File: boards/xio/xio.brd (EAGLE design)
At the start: 170 x 100 mm, 151 parts, among them Y2 NX3225SA-12.000MHZ-STD-CSR-1

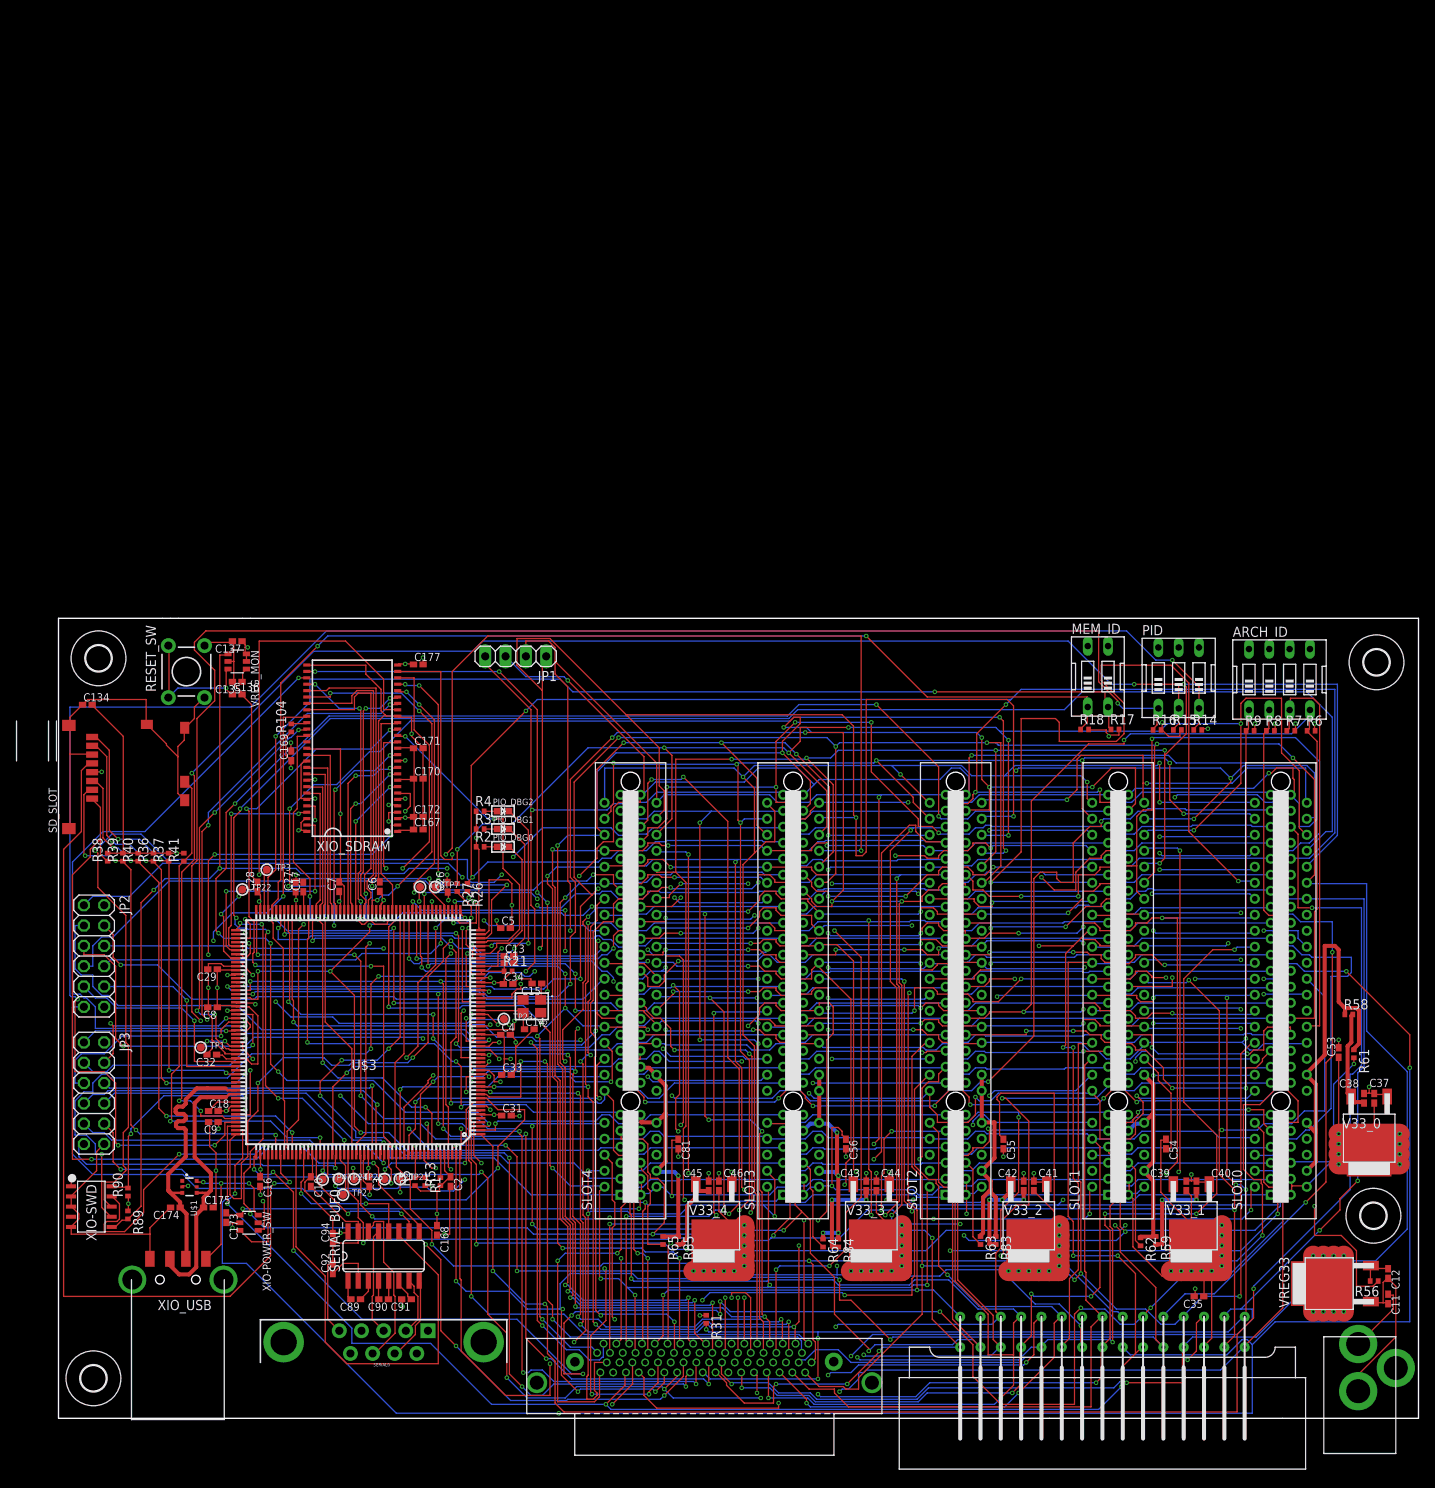
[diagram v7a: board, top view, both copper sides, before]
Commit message: Routed board with everything except the cartridge isolation
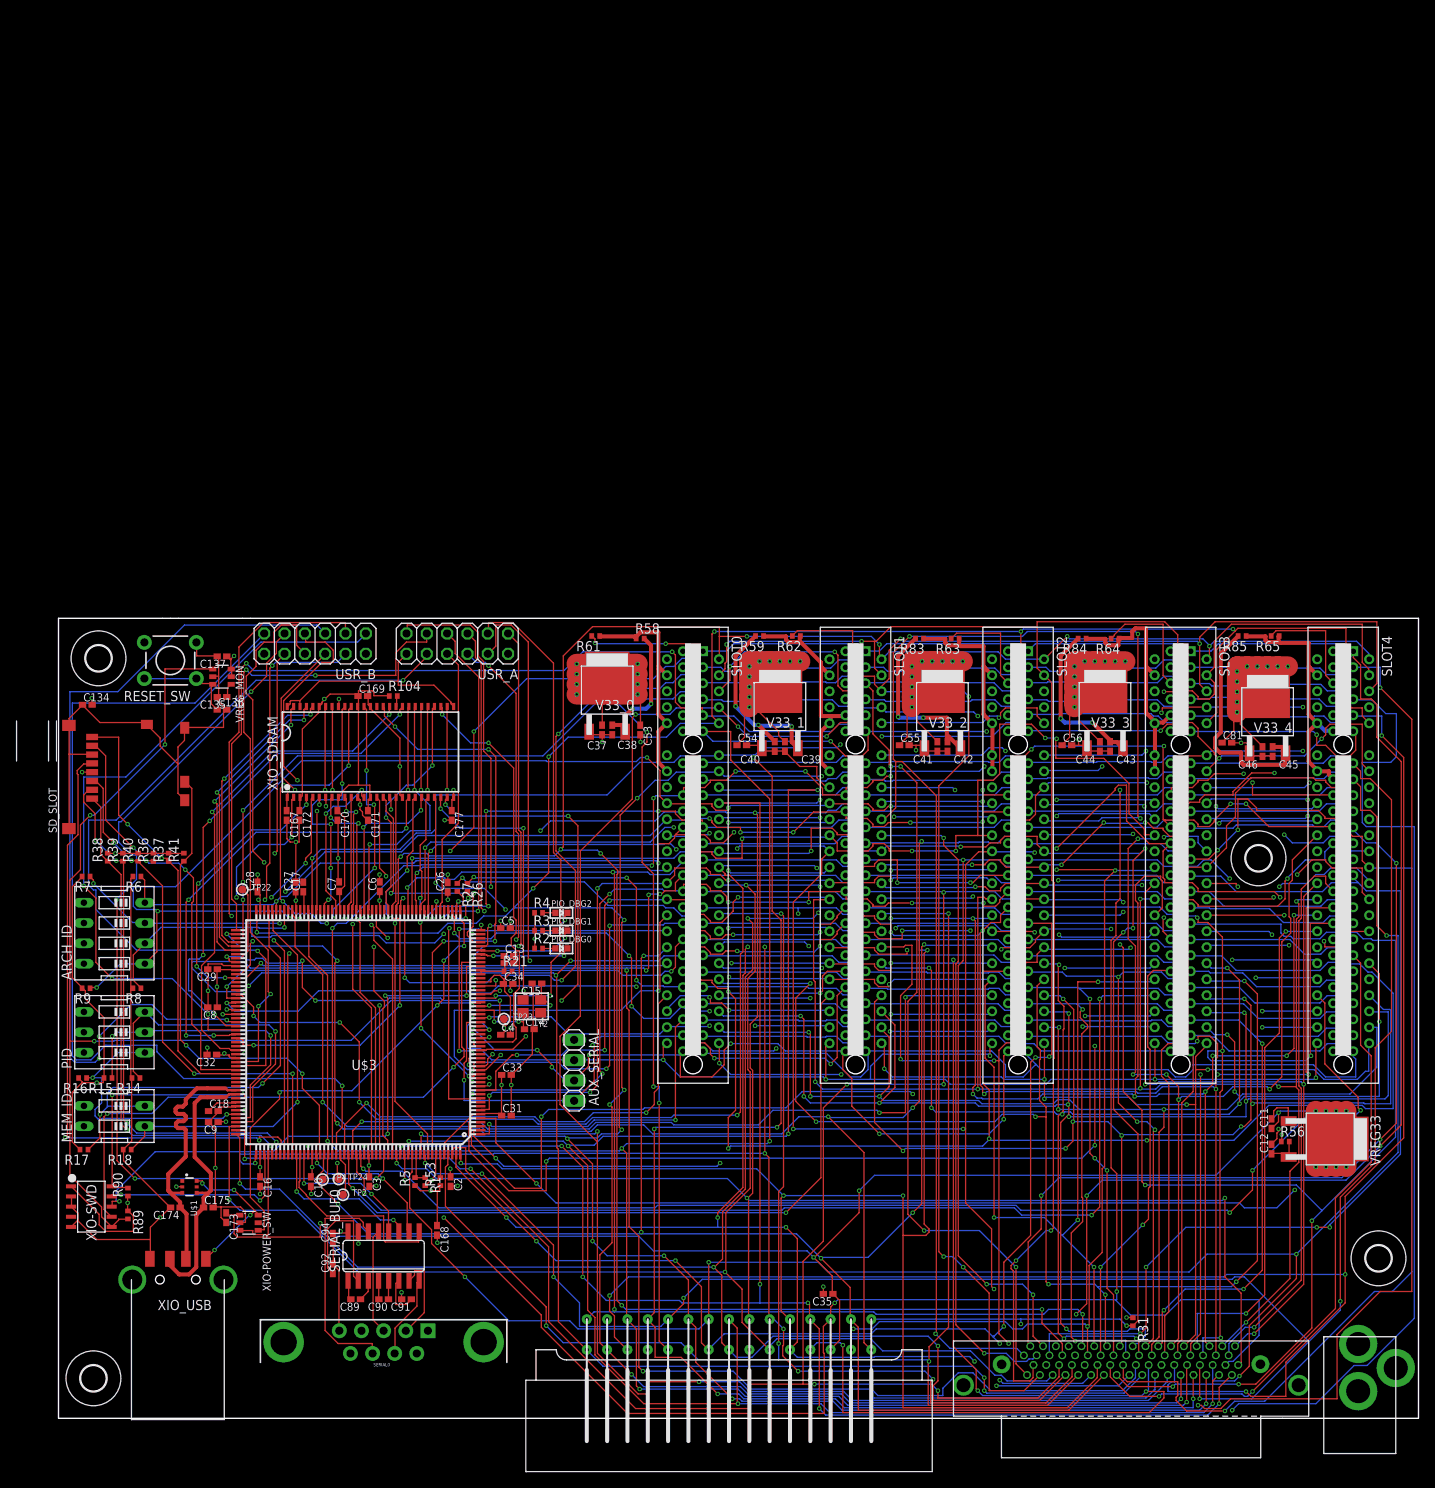
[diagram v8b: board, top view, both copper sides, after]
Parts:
- removed JP1: (no value), pinhead:1X04
- removed JP2, JP3: (no value), pinhead:2X06
- removed TP1, TP20, TP21, TP25, TP3, TP7, TP8: (no value), microbuilder:TESTPOINT_ROUND_1MM
- added AUX_SERIAL: (no value), pinhead:1X04
- added USR_A, USR_B: (no value), pinhead:2X06
- moved R7 151.7 mm to (3.45, 67.7), turned to 180 degrees
- moved ARCH_ID 149.0 mm to (6.99, 60.6), turned to 90 degrees
- moved R9 149.0 mm to (3.45, 53.8), turned to 180 degrees
- moved R6 147.9 mm to (9.80, 67.7), turned to 180 degrees
- moved R8 145.3 mm to (9.80, 53.8), turned to 180 degrees
- moved R16 141.2 mm to (3.01, 42.5), turned to 180 degrees
- moved R15 140.6 mm to (6.19, 42.5), turned to 180 degrees
- moved PID 140.2 mm to (6.99, 48.3), turned to 90 degrees
- moved R14 139.7 mm to (9.68, 42.5), turned to 180 degrees
- moved R17 139.2 mm to (3.19, 33.6), turned to 180 degrees
- moved MEM_ID 134.7 mm to (6.99, 37.8), turned to 90 degrees
- moved R18 130.7 mm to (8.59, 33.6), turned to 180 degrees
- moved V33_0 112.6 mm to (68.6, 93.0), turned to 0 degrees
- moved R61 108.2 mm to (67.2, 97.8), turned to 180 degrees
- moved R65 107.5 mm to (152.1, 97.8), turned to 180 degrees
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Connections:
- removed net N$107: TP20.P$1, U$3.9
- removed net N$108: TP21.P$1, U$3.111
- removed net N$112: TP25.P$1, U$3.133
- removed net N$3: TP1.P$1, U$3.134
- removed net N$5: TP3.P$1, U$3.102
- removed net N$86: TP7.P$1, U$3.50
- removed net N$93: TP8.P$1, U$3.8
- net +3V3: now also USR_A.2, USR_B.2; no longer JP2.2, JP3.2
- net AUX_CTS: now also AUX_SERIAL.1; no longer JP1.1
- net AUX_RTS: now also AUX_SERIAL.4; no longer JP1.4
- net AUX_RX: now also AUX_SERIAL.2; no longer JP1.2
- net AUX_TX: now also AUX_SERIAL.3; no longer JP1.3
- net GND: now also USR_A.12, USR_B.12; no longer JP2.12, JP3.12
- net USRA_CLK: now also USR_A.1; no longer JP2.1
- net USRA_D0: now also USR_A.3; no longer JP2.3
- net USRA_D1: now also USR_A.4; no longer JP2.4
- net USRA_D2: now also USR_A.5; no longer JP2.5
- net USRA_D3: now also USR_A.6; no longer JP2.6
- net USRA_D4: now also USR_A.7; no longer JP2.7
- net USRA_D5: now also USR_A.8; no longer JP2.8
- net USRA_D6: now also USR_A.9; no longer JP2.9
- net USRA_D7: now also USR_A.10; no longer JP2.10
- net USRA_MISC: now also USR_A.11; no longer JP2.11
- net USRB_CLK: now also USR_B.1; no longer JP3.1
- net USRB_D0: now also USR_B.3; no longer JP3.3
- net USRB_D1: now also USR_B.4; no longer JP3.4
- net USRB_D2: now also USR_B.5; no longer JP3.5
- net USRB_D3: now also USR_B.6; no longer JP3.6
- net USRB_D4: now also USR_B.7; no longer JP3.7
- net USRB_D5: now also USR_B.8; no longer JP3.8
- net USRB_D6: now also USR_B.9; no longer JP3.9
- net USRB_D7: now also USR_B.10; no longer JP3.10
- net USRB_MISC: now also USR_B.11; no longer JP3.11
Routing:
- net PID2: track 230.4 -> 41.2 mm, vias 4 -> 1
- net SPI_SS0: track 212.7 -> 39.0 mm, vias 4 -> 2
- net PID0: track 198.3 -> 32.8 mm, vias 3 -> 2
- net SPI_IRQ0: track 215.8 -> 59.8 mm, vias 5 -> 2
- net VHDCI_A0: track 229.5 -> 382.7 mm, vias 4 -> 7
- net PID1: track 188.7 -> 38.7 mm, vias 4 -> 2
- net AUX_CTS: track 257.8 -> 110.9 mm, vias 7 -> 6
- net !VHDCI_MPD!: track 166.5 -> 308.7 mm, vias 4 -> 5
- net VHDCI_A4: track 212.7 -> 340.9 mm, vias 5 -> 9
- net VHDCI_A6: track 192.3 -> 315.0 mm
- net VHDCI_S5: track 400.4 -> 278.7 mm, vias 10 -> 9
- net VHDCI_A8: track 192.6 -> 311.1 mm, vias 2 -> 5
- net VHDCI_A1: track 225.4 -> 339.9 mm, vias 6 -> 12
- net VHDCI_A2: track 295.5 -> 403.1 mm, vias 12 -> 7
- net SPI_CLK: track 245.9 -> 141.0 mm, vias 6 -> 5
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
